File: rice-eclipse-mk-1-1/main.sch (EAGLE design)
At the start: 56 parts, among them U1 LM1084ISX-5.0/NOPB, U2 THS4531IDRD8-M, U3 THS4531IDRD8-M, U4 THS4531IDRD8-M, U5 THS4531IDRD8-M, U6 1101M2S3CQE2, U7 1101M2S3CQE2, U8 1101M2S3CQE2, X1 2540-5

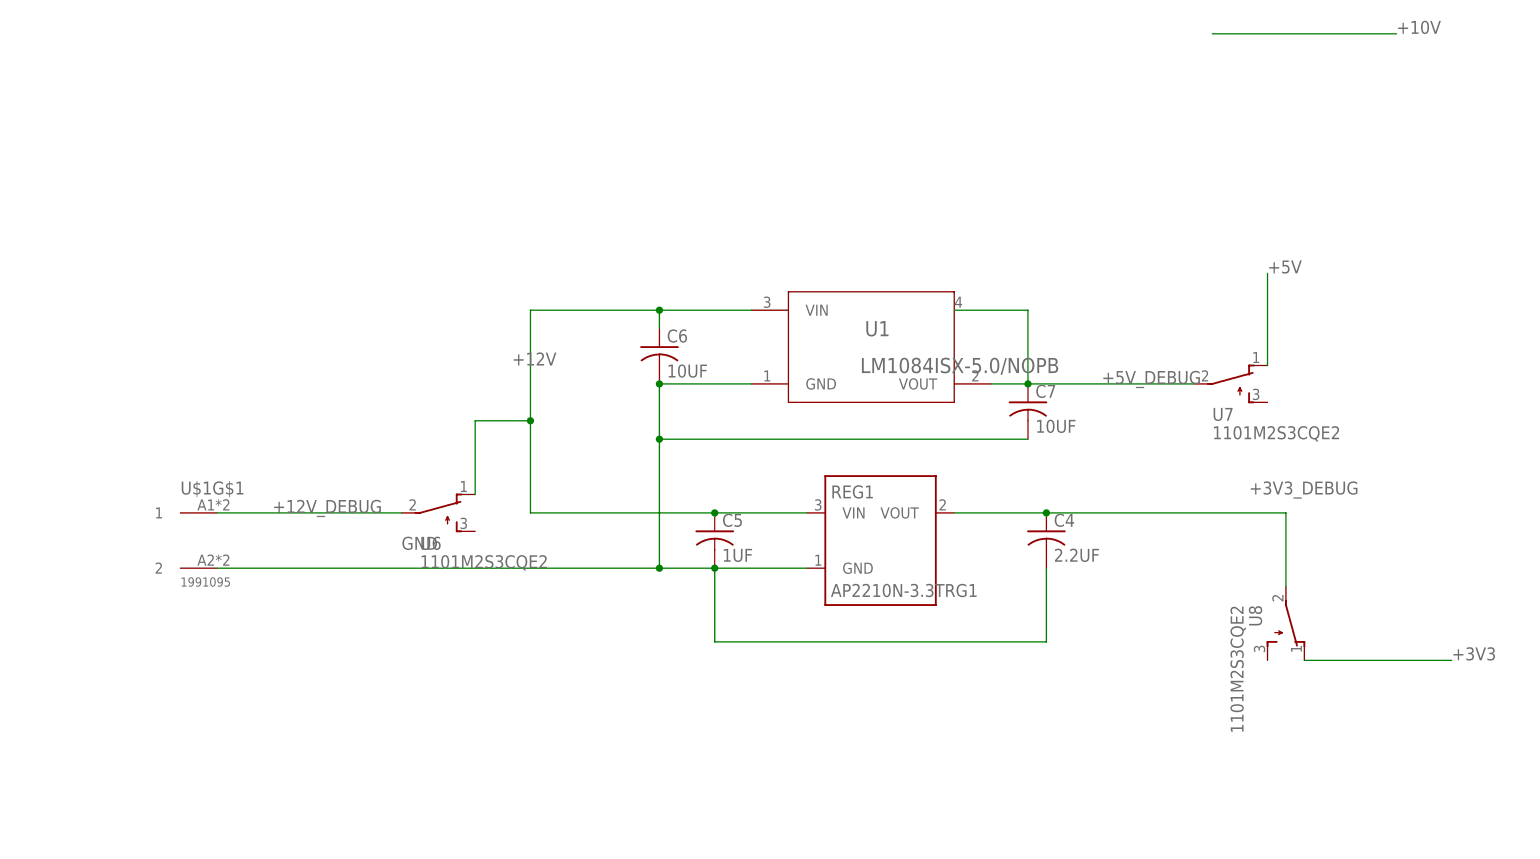
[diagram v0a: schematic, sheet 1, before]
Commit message: Added to the LEDs
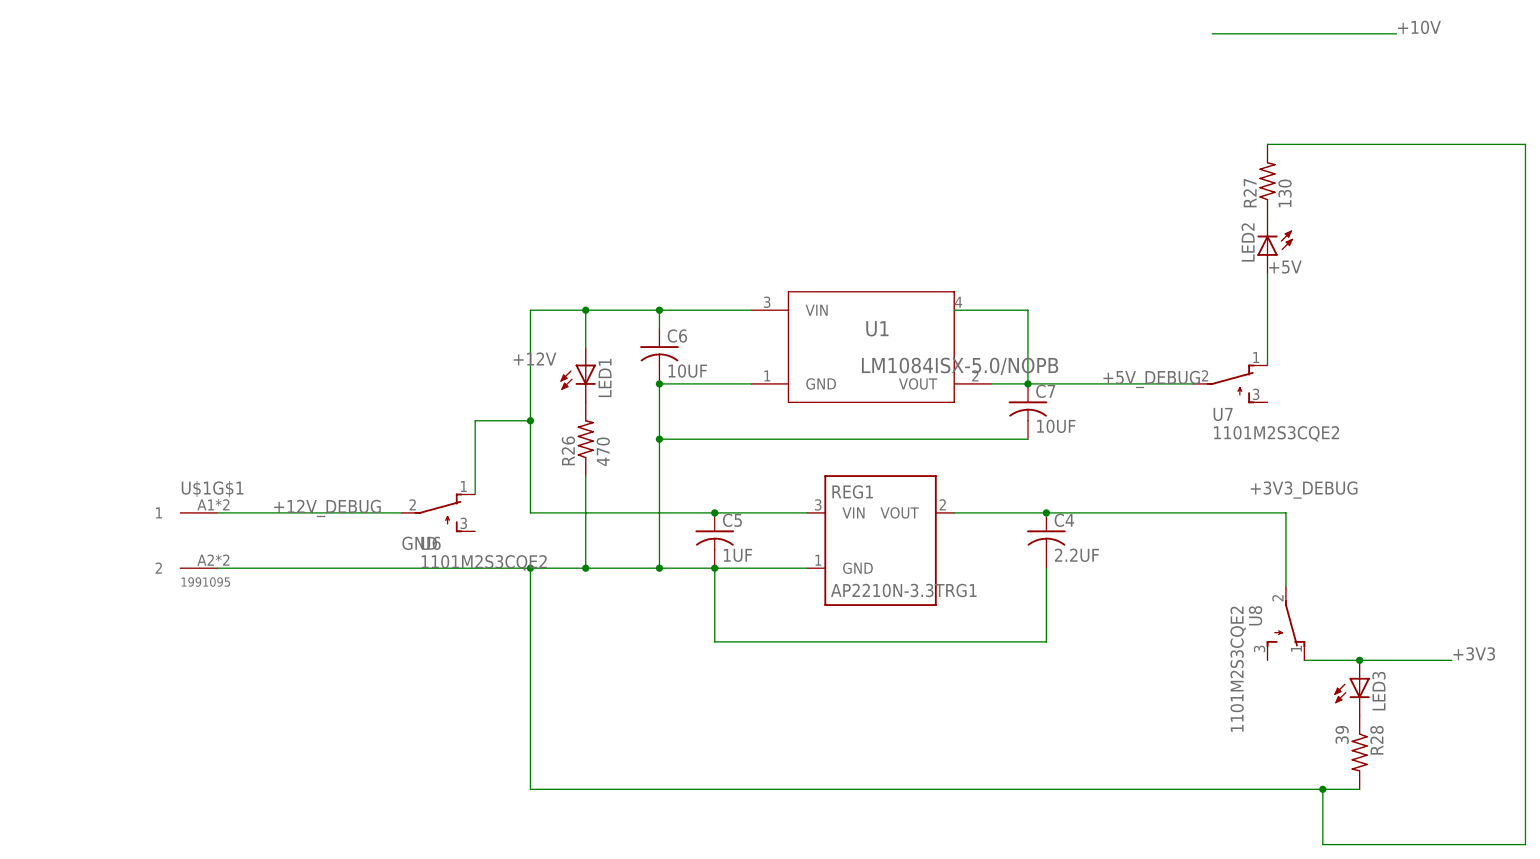
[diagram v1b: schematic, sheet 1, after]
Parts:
- added LED1, LED2, LED3: (no value), led:LED5MM
- added R26: 470, resistor:R-US_R0603
- added R27: 130, resistor:R-US_R0603
- added R28: 39, resistor:R-US_R0603
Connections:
- new net N$1: LED1.C, R26.2
- new net N$2: LED2.C, R27.1
- new net N$3: LED3.C, R28.1
- net +12V: now also LED1.A
- net +3V3: now also LED3.A
- net +5V: now also LED2.A
- net GND: now also R26.1, R27.2, R28.2
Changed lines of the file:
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@@
 <part name="U7" library="SLIDE_SW" deviceset="1101M2S3CQE2" device=""/>
 <part name="U8" library="SLIDE_SW" deviceset="1101M2S3CQE2" device=""/>
+<part name="LED1" library="led" library_urn="urn:adsk.eagle:library:259" deviceset="LED" device="5MM" package3d_urn="urn:adsk.eagle:package:15799/1"/>
+<part name="LED2" library="led" library_urn="urn:adsk.eagle:library:259" deviceset="LED" device="5MM" package3d_urn="urn:adsk.eagle:package:15799/1"/>
+<part name="LED3" library="led" library_urn="urn:adsk.eagle:library:259" deviceset="LED" device="5MM" package3d_urn="urn:adsk.eagle:package:15799/1"/>
+<part name="R26" library="resistor" library_urn="urn:adsk.eagle:library:348" deviceset="R-US_" device="R0603" package3d_urn="urn:adsk.eagle:package:26057/1" value="470"/>
+<part name="R27" library="resistor" library_urn="urn:adsk.eagle:library:348" deviceset="R-US_" device="R0603" package3d_urn="urn:adsk.eagle:package:26057/1" value="130"/>
+<part name="R28" library="resistor" library_urn="urn:adsk.eagle:library:348" deviceset="R-US_" device="R0603" package3d_urn="urn:adsk.eagle:package:26057/1" value="39"/>
 </parts>
 <sheets>
@@
 <instance part="U7" gate="A" x="198.12" y="111.76" rot="R270"/>
 <instance part="U8" gate="A" x="205.74" y="78.74" rot="R180"/>
+<instance part="LED1" gate="G$1" x="109.22" y="114.3"/>
+<instance part="LED2" gate="G$1" x="203.2" y="129.54" rot="R180"/>
+<instance part="LED3" gate="G$1" x="215.9" y="71.12"/>
+<instance part="R26" gate="G$1" x="109.22" y="104.14" rot="R90"/>
+<instance part="R27" gate="G$1" x="203.2" y="139.7" rot="R90"/>
+<instance part="R28" gate="G$1" x="215.9" y="60.96" rot="R270"/>
 </instances>
 <busses>
@@
 <label x="83.82" y="88.9" size="1.778" layer="95"/>
 <pinref part="U1" gate="A" pin="GND"/>
-<wire x1="119.38" y1="86.36" x2="58.42" y2="86.36" width="0.1524" layer="91"/>
+<wire x1="119.38" y1="86.36" x2="109.22" y2="86.36" width="0.1524" layer="91"/>
+<wire x1="109.22" y1="86.36" x2="101.6" y2="86.36" width="0.1524" layer="91"/>
+<wire x1="101.6" y1="86.36" x2="58.42" y2="86.36" width="0.1524" layer="91"/>
 <wire x1="132.08" y1="111.76" x2="119.38" y2="111.76" width="0.1524" layer="91"/>
 <wire x1="119.38" y1="111.76" x2="119.38" y2="104.14" width="0.1524" layer="91"/>
@@
 <wire x1="172.72" y1="76.2" x2="172.72" y2="86.36" width="0.1524" layer="91"/>
 <wire x1="119.38" y1="86.36" x2="127" y2="86.36" width="0.1524" layer="91"/>
+<pinref part="R26" gate="G$1" pin="1"/>
+<wire x1="109.22" y1="99.06" x2="109.22" y2="86.36" width="0.1524" layer="91"/>
+<junction x="109.22" y="86.36"/>
+<pinref part="R28" gate="G$1" pin="2"/>
+<wire x1="215.9" y1="55.88" x2="210.82" y2="55.88" width="0.1524" layer="91"/>
+<wire x1="210.82" y1="55.88" x2="101.6" y2="55.88" width="0.1524" layer="91"/>
+<wire x1="101.6" y1="55.88" x2="101.6" y2="86.36" width="0.1524" layer="91"/>
+<junction x="101.6" y="86.36"/>
+<pinref part="R27" gate="G$1" pin="2"/>
+<wire x1="203.2" y1="144.78" x2="238.76" y2="144.78" width="0.1524" layer="91"/>
+<wire x1="238.76" y1="144.78" x2="238.76" y2="48.26" width="0.1524" layer="91"/>
+<wire x1="238.76" y1="48.26" x2="210.82" y2="48.26" width="0.1524" layer="91"/>
+<wire x1="210.82" y1="48.26" x2="210.82" y2="55.88" width="0.1524" layer="91"/>
+<junction x="210.82" y="55.88"/>
 </segment>
 </net>
@@
 <pinref part="C6" gate="G$1" pin="1"/>
 <wire x1="119.38" y1="121.92" x2="119.38" y2="119.38" width="0.1524" layer="91"/>
-<wire x1="119.38" y1="121.92" x2="101.6" y2="121.92" width="0.1524" layer="91"/>
+<wire x1="119.38" y1="121.92" x2="109.22" y2="121.92" width="0.1524" layer="91"/>
 <junction x="119.38" y="121.92"/>
 <pinref part="U1" gate="A" pin="VIN"/>
+<wire x1="109.22" y1="121.92" x2="101.6" y2="121.92" width="0.1524" layer="91"/>
 <wire x1="132.08" y1="121.92" x2="119.38" y2="121.92" width="0.1524" layer="91"/>
 <label x="99.06" y="114.3" size="1.778" layer="95"/>
@@
 <pinref part="U6" gate="A" pin="O"/>
 <wire x1="93.98" y1="96.52" x2="93.98" y2="106.68" width="0.1524" layer="91"/>
+<pinref part="LED1" gate="G$1" pin="A"/>
+<wire x1="109.22" y1="121.92" x2="109.22" y2="116.84" width="0.1524" layer="91"/>
+<junction x="109.22" y="121.92"/>
 </segment>
 </net>
 <net name="+3V3" class="0">
 <segment>
-<wire x1="208.28" y1="73.66" x2="228.6" y2="73.66" width="0.1524" layer="91"/>
+<wire x1="208.28" y1="73.66" x2="215.9" y2="73.66" width="0.1524" layer="91"/>
 <label x="228.6" y="73.66" size="1.778" layer="95"/>
+<pinref part="LED3" gate="G$1" pin="A"/>
+<wire x1="215.9" y1="73.66" x2="228.6" y2="73.66" width="0.1524" layer="91"/>
+<junction x="215.9" y="73.66"/>
 </segment>
 </net>
@@
 <wire x1="203.2" y1="114.3" x2="203.2" y2="127" width="0.1524" layer="91"/>
 <label x="203.2" y="127" size="1.778" layer="95"/>
+<pinref part="LED2" gate="G$1" pin="A"/>
 </segment>
 </net>
@@
 </segment>
 </net>
+<net name="N$1" class="0">
+<segment>
+<pinref part="LED1" gate="G$1" pin="C"/>
+<pinref part="R26" gate="G$1" pin="2"/>
+</segment>
+</net>
+<net name="N$2" class="0">
+<segment>
+<pinref part="LED2" gate="G$1" pin="C"/>
+<pinref part="R27" gate="G$1" pin="1"/>
+</segment>
+</net>
+<net name="N$3" class="0">
+<segment>
+<pinref part="LED3" gate="G$1" pin="C"/>
+<pinref part="R28" gate="G$1" pin="1"/>
+</segment>
+</net>

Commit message: Cleaned up the board, added adcs, debug pins.
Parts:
- added ADC2, ADC3: MCP3208SN, microchip-extra:MCP3208SN
- added C1, C2: 1UF, rcl:C-USC0603
- added R29, R30: 500K, rcl:R-US_R0603
- added X2, X3: (no value), con-phoenix-250-extra:1770924
- added X4, X7, X8: (no value), con-phoenix-254:MPT8
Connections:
- new net ADC2_A0: ADC2.CH0, X7-1.1
- new net ADC2_A1: ADC2.CH1, X7-2.1
- new net ADC2_A2: ADC2.CH2, X7-3.1
- new net ADC2_A3: ADC2.CH3, X7-4.1
- new net ADC2_A4: ADC2.CH4, X7-5.1
- new net ADC2_A5: ADC2.CH5, X7-6.1
- new net ADC2_A6: ADC2.CH6, X7-7.1
- new net ADC2_A7: ADC2.CH7, X7-8.1
- new net ADC3_A0: ADC3.CH0, X8-1.1
- new net ADC3_A1: ADC3.CH1, X8-2.1
- new net ADC3_A2: ADC3.CH2, X8-3.1
- new net ADC3_A3: ADC3.CH3, X8-4.1
- new net ADC3_A4: ADC3.CH4, X8-5.1
- new net ADC3_A5: ADC3.CH5, X8-6.1
- new net ADC3_A6: ADC3.CH6, X8-7.1
- new net ADC3_A7: ADC3.CH7, X8-8.1
- net +3V3: now also ADC2.VDD, ADC2.VREF, ADC3.VDD, ADC3.VREF, C1.1, C2.1, R29.2, R30.2, U8.O
- net +5V: now also U7.O
- net ADC1_A0: now also R11.2, U2.VOUT-, X4-1.1; no longer R14.2, U2.VOUT+
- net ADC1_A1: now also R14.2, U2.VOUT+, X4-2.1; no longer R11.2, U2.VOUT-
- net ADC1_A2: now also R15.2, U3.VOUT-, X4-3.1; no longer R16.2, U3.VOUT+
- net ADC1_A3: now also R16.2, U3.VOUT+, X4-4.1; no longer R15.2, U3.VOUT-
- net ADC1_A4: now also R19.2, U4.VOUT-, X4-5.1; no longer R20.2, U4.VOUT+
- net ADC1_A5: now also R20.2, U4.VOUT+, X4-6.1; no longer R19.2, U4.VOUT-
- net ADC1_A6: now also R23.2, U5.VOUT-, X4-7.1; no longer R24.2, U5.VOUT+
- net ADC1_A7: now also R24.2, U5.VOUT+, X4-8.1; no longer R23.2, U5.VOUT-
- net ADC1_CS: now also ADC1.CS*
- net ADC2_CS: now also ADC2.CS*, R29.1
- net ADC3_CS: now also ADC3.CS*, R30.1
- net GND: now also ADC2.AGND, ADC2.DGND, ADC3.AGND, ADC3.DGND, C1.2, C2.2
- net LC_1_OUT+: now also X6-3.SK; no longer X5-1.SK
- net LC_1_OUT-: now also X6-4.SK; no longer X5-2.SK
- net LC_2_OUT+: now also X6-1.SK; no longer X5-3.SK
- net LC_2_OUT-: now also X6-2.SK; no longer X5-4.SK
- net LC_3_OUT+: now also X5-3.SK; no longer X6-1.SK
- net LC_3_OUT-: now also X5-4.SK; no longer X6-2.SK
- net LC_4_OUT+: now also X5-1.SK; no longer X6-3.SK
- net LC_4_OUT-: now also X5-2.SK; no longer X6-4.SK
- net MISO: now also ADC1.DOUT, ADC2.DOUT, ADC3.DOUT
- net MOSI: now also ADC1.DIN, ADC2.DIN, ADC3.DIN
- net SCLK: now also ADC1.CLK, ADC2.CLK, ADC3.CLK
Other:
- note added: "ADC_1 Debug pins"

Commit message: Added more board parts.
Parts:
- removed U7, U8: 1101M2S3CQE2, SLIDE_SW:1101M2S3CQE2
- added IC1, IC2, IC3, IC4: LMV321LICTRT, st-microelectronics-extra:LMV321LICTRT
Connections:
- removed net +3V3_DEBUG: C4.1, REG1.VOUT, U8.P
- removed net +5V_DEBUG: C7.1, U1.4, U1.VOUT, U7.P
- net +3V3: now also C4.1, REG1.VOUT; no longer U8.O
- net +5V: now also C7.1, U1.4, U1.VOUT; no longer U7.O
- net ADC2_A0: now also X2-6.SK
- net ADC2_A1: now also X2-5.SK
- net ADC2_A2: now also X2-4.SK
- net ADC2_A3: now also X2-3.SK
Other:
- note added: "TC_1"
- note added: "TC_2"
- note added: "TC_3"
- note added: "TC_4"
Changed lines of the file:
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@@
 <layer number="51" name="tDocu" color="7" fill="1" visible="no" active="no"/>
 <layer number="52" name="bDocu" color="7" fill="1" visible="no" active="no"/>
+<layer number="88" name="SimResults" color="9" fill="1" visible="yes" active="yes"/>
+<layer number="89" name="SimProbes" color="9" fill="1" visible="yes" active="yes"/>
 <layer number="90" name="Modules" color="5" fill="1" visible="yes" active="yes"/>
 <layer number="91" name="Nets" color="2" fill="1" visible="yes" active="yes"/>
@@
 <part name="X6" library="con-phoenix-250-extra" deviceset="1770908" device=""/>
 <part name="U6" library="SLIDE_SW" deviceset="1101M2S3CQE2" device=""/>
-<part name="U7" library="SLIDE_SW" deviceset="1101M2S3CQE2" device=""/>
-<part name="U8" library="SLIDE_SW" deviceset="1101M2S3CQE2" device=""/>
 <part name="LED1" library="led" library_urn="urn:adsk.eagle:library:259" deviceset="LED" device="5MM" package3d_urn="urn:adsk.eagle:package:15799/1"/>
 <part name="LED2" library="led" library_urn="urn:adsk.eagle:library:259" deviceset="LED" device="5MM" package3d_urn="urn:adsk.eagle:package:15799/1"/>
@@
 <part name="X7" library="con-phoenix-254" library_urn="urn:adsk.eagle:library:172" deviceset="MPT8" device="" package3d_urn="urn:adsk.eagle:package:9329/1"/>
 <part name="X8" library="con-phoenix-254" library_urn="urn:adsk.eagle:library:172" deviceset="MPT8" device="" package3d_urn="urn:adsk.eagle:package:9329/1"/>
+<part name="FRAME10" library="frames" library_urn="urn:adsk.eagle:library:229" deviceset="A4L-LOC" device=""/>
+<part name="FRAME11" library="frames" library_urn="urn:adsk.eagle:library:229" deviceset="A4L-LOC" device=""/>
+<part name="IC1" library="st-microelectronics-extra" deviceset="LMV321LICT" device="RT"/>
+<part name="IC2" library="st-microelectronics-extra" deviceset="LMV321LICT" device="RT"/>
+<part name="IC3" library="st-microelectronics-extra" deviceset="LMV321LICT" device="RT"/>
+<part name="IC4" library="st-microelectronics-extra" deviceset="LMV321LICT" device="RT"/>
 </parts>
 <sheets>
@@
 <instance part="U$1" gate="G$2" x="58.42" y="86.36"/>
 <instance part="U6" gate="A" x="88.9" y="93.98" rot="R270"/>
-<instance part="U7" gate="A" x="198.12" y="111.76" rot="R270"/>
-<instance part="U8" gate="A" x="205.74" y="78.74" rot="R180"/>
 <instance part="LED1" gate="G$1" x="109.22" y="114.3"/>
 <instance part="LED2" gate="G$1" x="203.2" y="129.54" rot="R180"/>
@@
 <pinref part="LED3" gate="G$1" pin="A"/>
 <wire x1="215.9" y1="73.66" x2="228.6" y2="73.66" width="0.1524" layer="91"/>
-<pinref part="U8" gate="A" pin="O"/>
-<wire x1="215.9" y1="73.66" x2="208.28" y2="73.66" width="0.1524" layer="91"/>
+<wire x1="215.9" y1="73.66" x2="210.82" y2="73.66" width="0.1524" layer="91"/>
 <junction x="215.9" y="73.66"/>
-</segment>
-</net>
-<net name="+5V" class="0">
-<segment>
-<label x="203.2" y="127" size="1.778" layer="95"/>
-<pinref part="LED2" gate="G$1" pin="A"/>
-<pinref part="U7" gate="A" pin="O"/>
-<wire x1="203.2" y1="114.3" x2="203.2" y2="127" width="0.1524" layer="91"/>
+<wire x1="210.82" y1="73.66" x2="210.82" y2="93.98" width="0.1524" layer="91"/>
+<wire x1="160.02" y1="93.98" x2="172.72" y2="93.98" width="0.1524" layer="91"/>
+<label x="200.66" y="96.52" size="1.778" layer="95"/>
+<pinref part="REG1" gate="G$1" pin="VOUT"/>
+<pinref part="C4" gate="G$1" pin="1"/>
+<wire x1="172.72" y1="93.98" x2="210.82" y2="93.98" width="0.1524" layer="91"/>
+<junction x="172.72" y="93.98"/>
 </segment>
 </net>
@@
 </segment>
 </net>
-<net name="+5V_DEBUG" class="0">
+<net name="N$1" class="0">
+<segment>
+<pinref part="LED1" gate="G$1" pin="C"/>
+<pinref part="R26" gate="G$1" pin="2"/>
+</segment>
+</net>
+<net name="N$2" class="0">
+<segment>
+<pinref part="LED2" gate="G$1" pin="C"/>
+<pinref part="R27" gate="G$1" pin="1"/>
+</segment>
+</net>
+<net name="N$3" class="0">
+<segment>
+<pinref part="LED3" gate="G$1" pin="C"/>
+<pinref part="R28" gate="G$1" pin="1"/>
+</segment>
+</net>
+<net name="+5V" class="0">
 <segment>
 <label x="180.34" y="111.76" size="1.778" layer="95"/>
@@
 <pinref part="C7" gate="G$1" pin="1"/>
 <junction x="170.18" y="111.76"/>
-<wire x1="170.18" y1="111.76" x2="193.04" y2="111.76" width="0.1524" layer="91"/>
+<wire x1="170.18" y1="111.76" x2="190.5" y2="111.76" width="0.1524" layer="91"/>
 <wire x1="165.1" y1="111.76" x2="170.18" y2="111.76" width="0.1524" layer="91"/>
 <pinref part="U1" gate="A" pin="4"/>
 <wire x1="160.02" y1="121.92" x2="170.18" y2="121.92" width="0.1524" layer="91"/>
 <wire x1="170.18" y1="121.92" x2="170.18" y2="111.76" width="0.1524" layer="91"/>
-<pinref part="U7" gate="A" pin="P"/>
-</segment>
-</net>
-<net name="+3V3_DEBUG" class="0">
-<segment>
-<wire x1="160.02" y1="93.98" x2="172.72" y2="93.98" width="0.1524" layer="91"/>
-<label x="200.66" y="96.52" size="1.778" layer="95"/>
-<pinref part="REG1" gate="G$1" pin="VOUT"/>
-<pinref part="C4" gate="G$1" pin="1"/>
-<wire x1="172.72" y1="93.98" x2="205.74" y2="93.98" width="0.1524" layer="91"/>
-<junction x="172.72" y="93.98"/>
-<wire x1="205.74" y1="93.98" x2="205.74" y2="83.82" width="0.1524" layer="91"/>
-<pinref part="U8" gate="A" pin="P"/>
-</segment>
-</net>
-<net name="N$1" class="0">
-<segment>
-<pinref part="LED1" gate="G$1" pin="C"/>
-<pinref part="R26" gate="G$1" pin="2"/>
-</segment>
-</net>
-<net name="N$2" class="0">
-<segment>
-<pinref part="LED2" gate="G$1" pin="C"/>
-<pinref part="R27" gate="G$1" pin="1"/>
-</segment>
-</net>
-<net name="N$3" class="0">
-<segment>
-<pinref part="LED3" gate="G$1" pin="C"/>
-<pinref part="R28" gate="G$1" pin="1"/>
+<wire x1="190.5" y1="111.76" x2="190.5" y2="121.92" width="0.1524" layer="91"/>
+<label x="203.2" y="127" size="1.778" layer="95"/>
+<pinref part="LED2" gate="G$1" pin="A"/>
+<wire x1="203.2" y1="121.92" x2="203.2" y2="127" width="0.1524" layer="91"/>
+<wire x1="190.5" y1="121.92" x2="203.2" y2="121.92" width="0.1524" layer="91"/>
 </segment>
 </net>
@@
 </sheet>
 <sheet>
+<description>&lt;b&gt;PT Amplification&lt;/b&gt;&lt;br&gt;
+Circuits for measuring PT</description>
+<plain>
+</plain>
+<instances>
+<instance part="FRAME10" gate="G$1" x="0" y="0" smashed="yes">
+<attribute name="DRAWING_NAME" x="217.17" y="15.24" size="2.54" layer="94"/>
+<attribute name="LAST_DATE_TIME" x="217.17" y="10.16" size="2.286" layer="94"/>
+<attribute name="SHEET" x="230.505" y="5.08" size="2.54" layer="94"/>
+</instance>
+<instance part="FRAME11" gate="G$1" x="0" y="0" smashed="yes">
+<attribute name="DRAWING_NAME" x="217.17" y="15.24" size="2.54" layer="94"/>
+<attribute name="LAST_DATE_TIME" x="217.17" y="10.16" size="2.286" layer="94"/>
+<attribute name="SHEET" x="230.505" y="5.08" size="2.54" layer="94"/>
+</instance>
+<instance part="IC1" gate="G$" x="53.34" y="129.54"/>
+<instance part="IC2" gate="G$" x="193.04" y="132.08"/>
+<instance part="IC3" gate="G$" x="53.34" y="88.9"/>
+<instance part="IC4" gate="G$" x="195.58" y="83.82"/>
+</instances>
+<busses>
+</busses>
+<nets>
+</nets>
+</sheet>
+<sheet>
 <description>&lt;title&gt;ADC&lt;/title&gt;
 The updated schematic for the adc because the old one is on backorder.</description>
@@
 <text x="73.66" y="170.18" size="2.54" layer="97">External Power Connectors</text>
 <text x="71.12" y="127" size="1.778" layer="97">TODO: Figure out how to properly distinguish these on the hardware board?</text>
+<text x="55.88" y="96.52" size="1.778" layer="97">TC_1</text>
+<text x="55.88" y="101.6" size="1.778" layer="97">TC_2</text>
+<text x="55.88" y="106.68" size="1.778" layer="97">TC_3</text>
+<text x="55.88" y="111.76" size="1.778" layer="97">TC_4</text>
 </plain>
 <instances>
@@
 </segment>
 </net>
+<net name="ADC2_A0" class="0">
+<segment>
+<pinref part="X2" gate="-6" pin="SK"/>
+<wire x1="30.48" y1="96.52" x2="43.18" y2="96.52" width="0.1524" layer="91"/>
+<label x="43.18" y="96.52" size="1.778" layer="95"/>
+</segment>
+</net>
+<net name="ADC2_A1" class="0">
+<segment>
+<pinref part="X2" gate="-5" pin="SK"/>
+<wire x1="30.48" y1="101.6" x2="43.18" y2="101.6" width="0.1524" layer="91"/>
+<label x="43.18" y="101.6" size="1.778" layer="95"/>
+</segment>
+</net>
+<net name="ADC2_A2" class="0">
+<segment>
+<pinref part="X2" gate="-4" pin="SK"/>
+<wire x1="30.48" y1="106.68" x2="43.18" y2="106.68" width="0.1524" layer="91"/>
+<label x="43.18" y="106.68" size="1.778" layer="95"/>
+</segment>
+</net>
+<net name="ADC2_A3" class="0">
+<segment>
+<pinref part="X2" gate="-3" pin="SK"/>
+<wire x1="30.48" y1="111.76" x2="43.18" y2="111.76" width="0.1524" layer="91"/>
+<label x="43.18" y="111.76" size="1.778" layer="95"/>
+</segment>
+</net>
